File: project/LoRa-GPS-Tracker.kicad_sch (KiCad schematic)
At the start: 57 parts, among them IC101 MCP73831-2-OT, IC102 MCP100-300D, IC103 FT230XS, IC104 NCP705MT30TCG, M101 SIM28ML, M102 RAK3172, Q101 BSS123, Q102 TP0610K, Q103 BSH205G2VL, SW102 ON/OFF, X101 DEBUG, X102 Conn_Coaxial, X103 BATTERY, X3 DEBUG

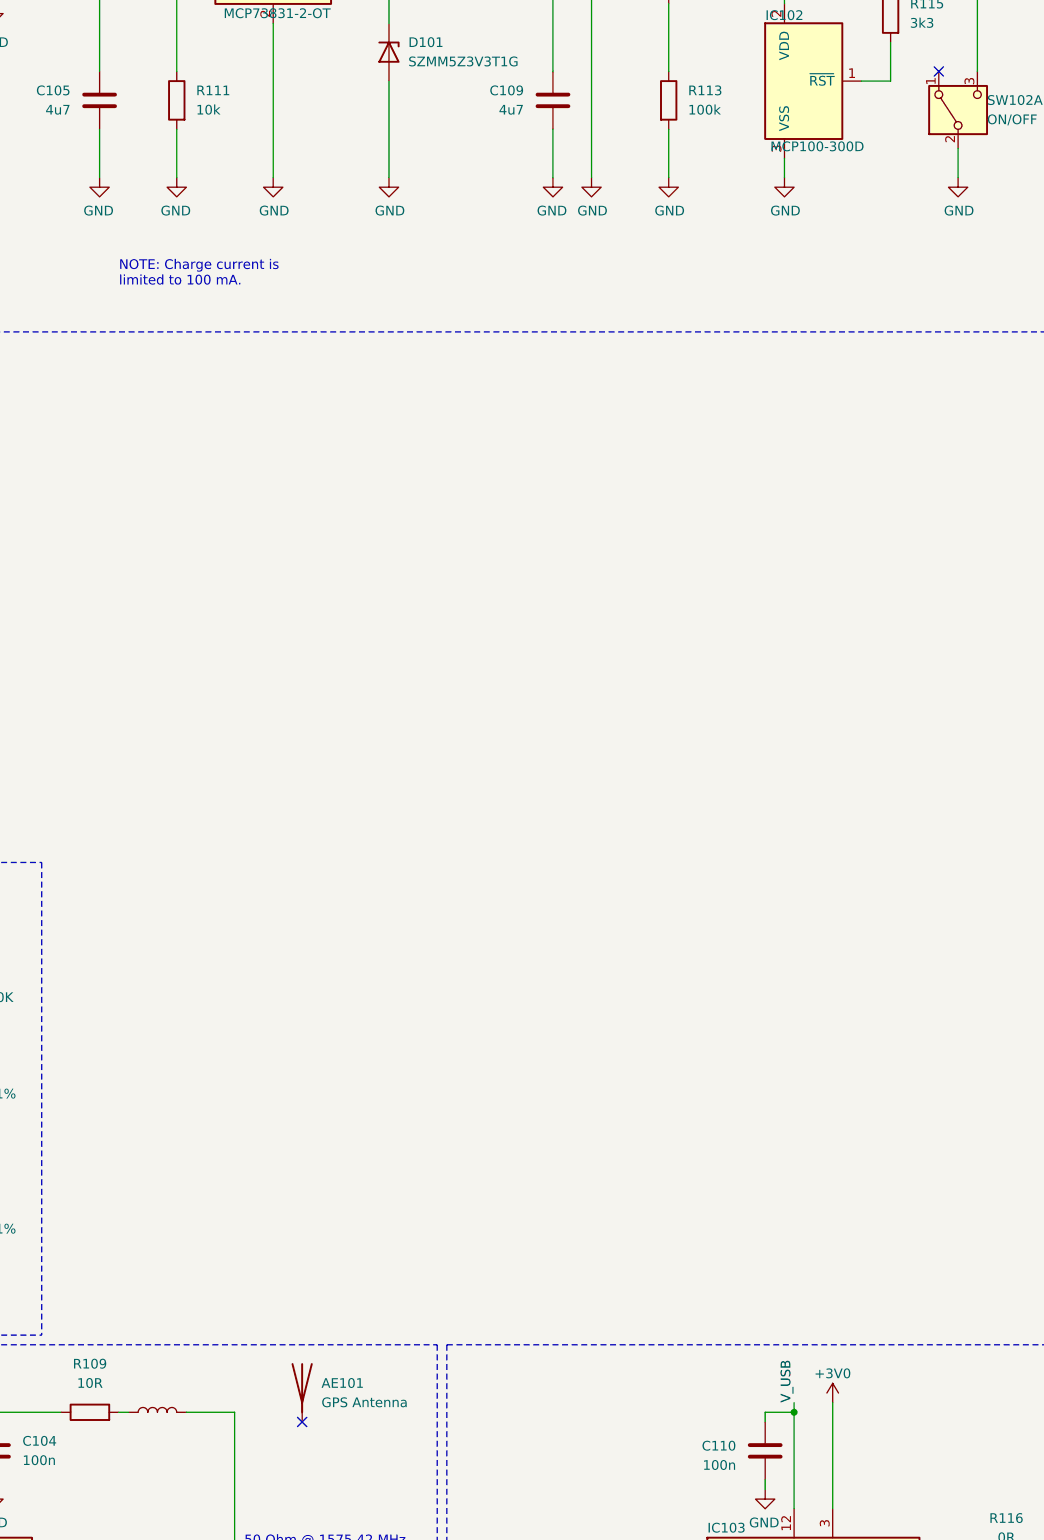
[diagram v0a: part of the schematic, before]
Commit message: Add missing part numbers and datasheets
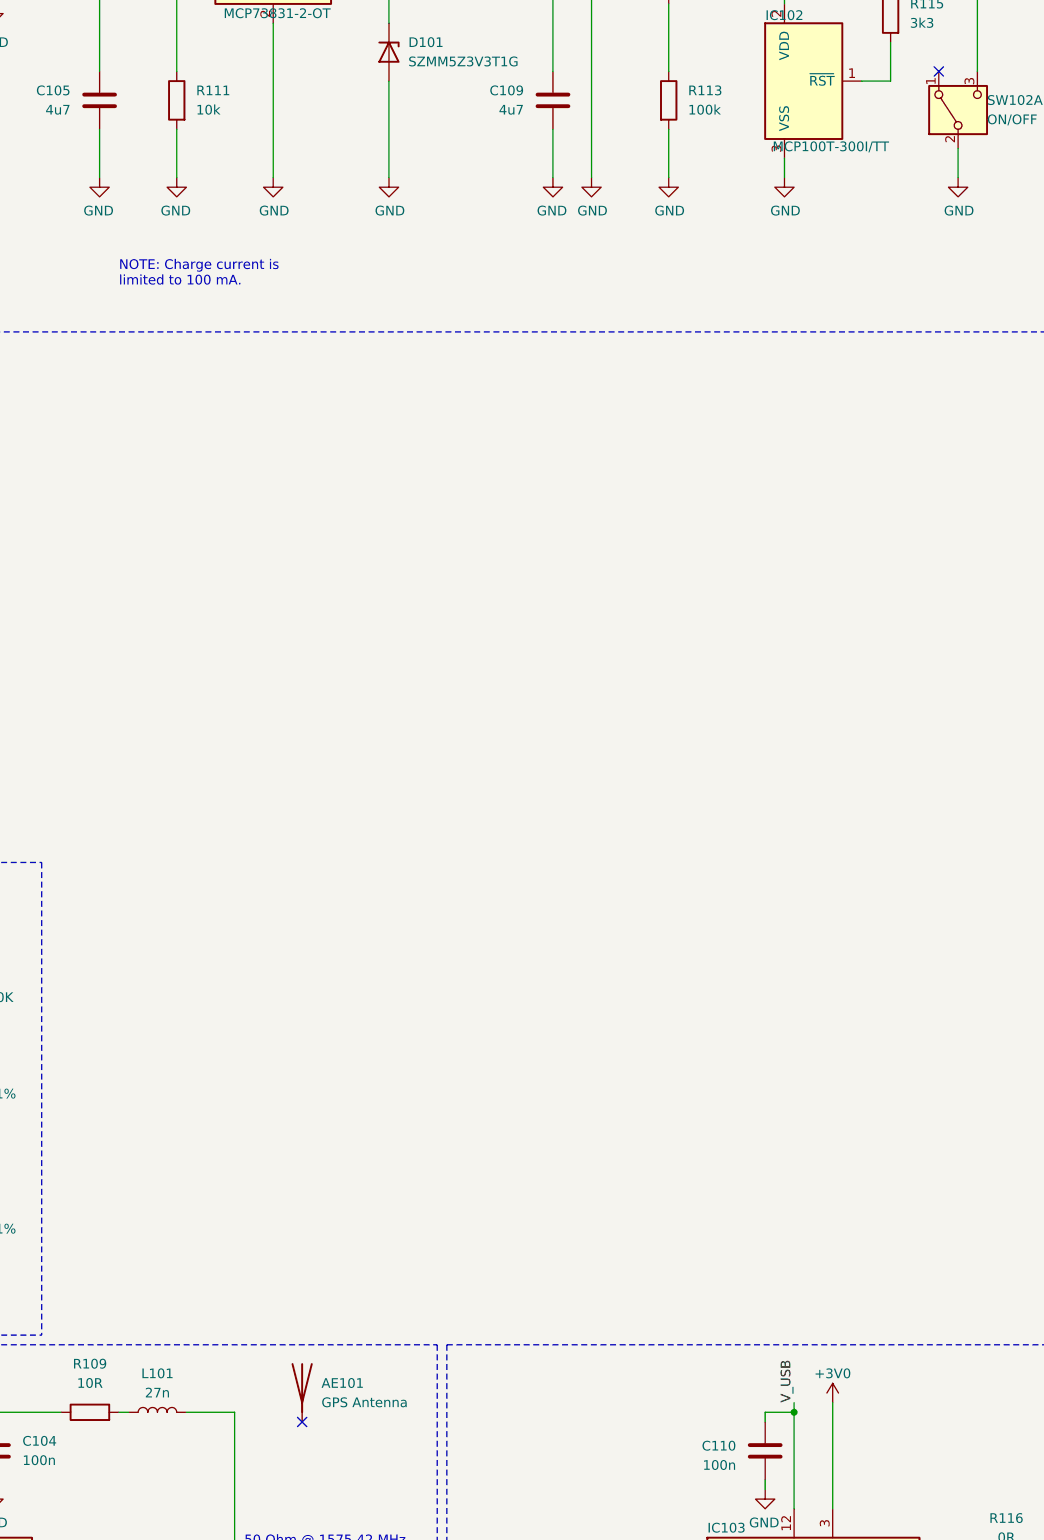
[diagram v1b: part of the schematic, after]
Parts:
- IC102: value MCP100-300D -> MCP100T-300I/TT
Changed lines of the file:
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@@
 			)
 		)
-		(property "Value" "MCP100-300D"
-			(at 174.498 59.436 0)
+		(property "Value" "MCP100T-300I/TT"
+			(at 176.276 59.436 0)
 			(effects
 				(font
@@
 			)
 		)
-		(property "Datasheet" "~"
+		(property "Datasheet" "https://www.mouser.de/datasheet/2/40/AVX_E_1004627-3313018.pdf"
 			(at 106.68 222.25 0)
 			(effects
@@
 		(fields_autoplaced yes)
 		(property "Reference" "L101"
-			(at 87.63 226.06 0)
+			(at 87.63 220.98 90)
 			(effects
 				(font
 					(size 1.27 1.27)
 				)
-				(hide yes)
 			)
 		)
 		(property "Value" "27n"
-			(at 87.63 226.06 0)
+			(at 87.63 223.52 90)
 			(effects
 				(font
 					(size 1.27 1.27)
 				)
-				(hide yes)
 			)
 		)
@@
 			(at 87.63 226.06 0)
 			(effects
+				(font
+					(size 1.27 1.27)
+				)
+				(hide yes)
+			)
+		)
+		(property "CONFIG" ""
+			(at 87.63 226.06 0)
+			(effects

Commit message: Make it possible to power cycle the GPS module
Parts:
- added Q104: TP0610K, Package_TO_SOT_SMD:SOT-23, symbol Transistor_FET:BSS84
- added R122: 100k, Resistor_SMD:R_0402_1005Metric_Pad0.72x0.64mm_HandSolder, symbol Device:R
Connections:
- net +3V0: now also Q104.2 (S), R122.1; no longer C101.1, C102.1, M101.8 (VCC)
- net GPS_E: now reaches M102.3 (ADC5)
- net GPS_E: now also Q104.1 (G), R122.2
- new net: C101.1, C102.1, M101.8 (VCC), Q104.3 (D)
- no-connect marks 29 -> 28
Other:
- moved on the sheet: C103, Q101, Q102, R101, R104, R105, R106

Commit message: Add I2C accelerometer
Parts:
- added C112: 100n, Capacitor_SMD:C_0402_1005Metric_Pad0.74x0.62mm_HandSolder, symbol Device:C
- added IC105: LIS2DH, Package_LGA:LGA-14_2x2mm_P0.35mm_LayoutBorder3x4y, symbol Sensor_Motion:LIS2DH
- added R115, R117: 3k3, Resistor_SMD:R_0402_1005Metric_Pad0.72x0.64mm_HandSolder, symbol Device:R
- R101: renamed from R102; Mfr. Bourns -> Vishay / Dale; Mfr. No. CR0805-J/-000ELF -> CRCW04020000Z0EDC; Order Number 652-CR0805-J/-000ELF -> 71-CRCW04020000Z0EDC
- R102: renamed from R103; Mfr. Bourns -> Vishay / Dale; Mfr. No. CR0805-J/-000ELF -> CRCW04020000Z0EDC; Order Number 652-CR0805-J/-000ELF -> 71-CRCW04020000Z0EDC
- R107: renamed from R110; Mfr. Bourns -> Vishay / Dale; Mfr. No. CR0805-J/-000ELF -> CRCW04020000Z0EDC; Order Number 652-CR0805-J/-000ELF -> 71-CRCW04020000Z0EDC
- R113: renamed from R116; Mfr. Bourns -> Vishay / Dale; Mfr. No. CR0805-J/-000ELF -> CRCW04020000Z0EDC; Order Number 652-CR0805-J/-000ELF -> 71-CRCW04020000Z0EDC
- R114: renamed from R117; Mfr. Bourns -> Vishay / Dale; Mfr. No. CR0805-J/-000ELF -> CRCW04020000Z0EDC; Order Number 652-CR0805-J/-000ELF -> 71-CRCW04020000Z0EDC
- R118: renamed from R101; now fitted
- X102: Mfr. Molex -> TE Connectivity / Linx Technologies; Mfr. No. 73412-0110 -> CONMHF1-SMD-G-T; Order Number 538-73412-0110 -> 712-CONMHF1-SMD-G-T
- renumbered C104 to C103, C105 to C104, C106 to C105, C107 to C106, C108 to C107, C109 to C108, C110 to C109, C111 to C110, C112 to C111, C103 to C115, D103 to D102, Q104 to Q101, Q103 to Q102, Q101 to Q103, Q102 to Q104, R122 to R103, R107 to R104, R108 to R105, R109 to R106, R111 to R108, R112 to R109, R113 to R110, R114 to R111, R115 to R112, R118 to R116, R120 to R119, R119 to R120, R104 to R121, R121 to R122, R105 to R123, R106 to R124, SW102 to SW101
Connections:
- net +3V0: now also C112.1, IC105.4 (~{CS}), IC105.7 (Vdd_IO), IC105.8 (Vdd), R115.1, R117.1
- net GND: now also C112.2, IC105.10 (GND), IC105.11 (GND), IC105.12 (GND), IC105.13 (GND), IC105.14 (GND), IC105.9 (GND)
- net at M102.10 (SDA): now also IC105.2 (SDA/SDI), R117.2
- net INT: now reaches M102.26 (ADC3)
- net INT: now also IC105.6 (INT1)
- net at M102.9 (SCL): now also IC105.1 (SCL/SPC), R115.2
- no-connect marks 28 -> 27
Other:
- moved on the sheet: C104

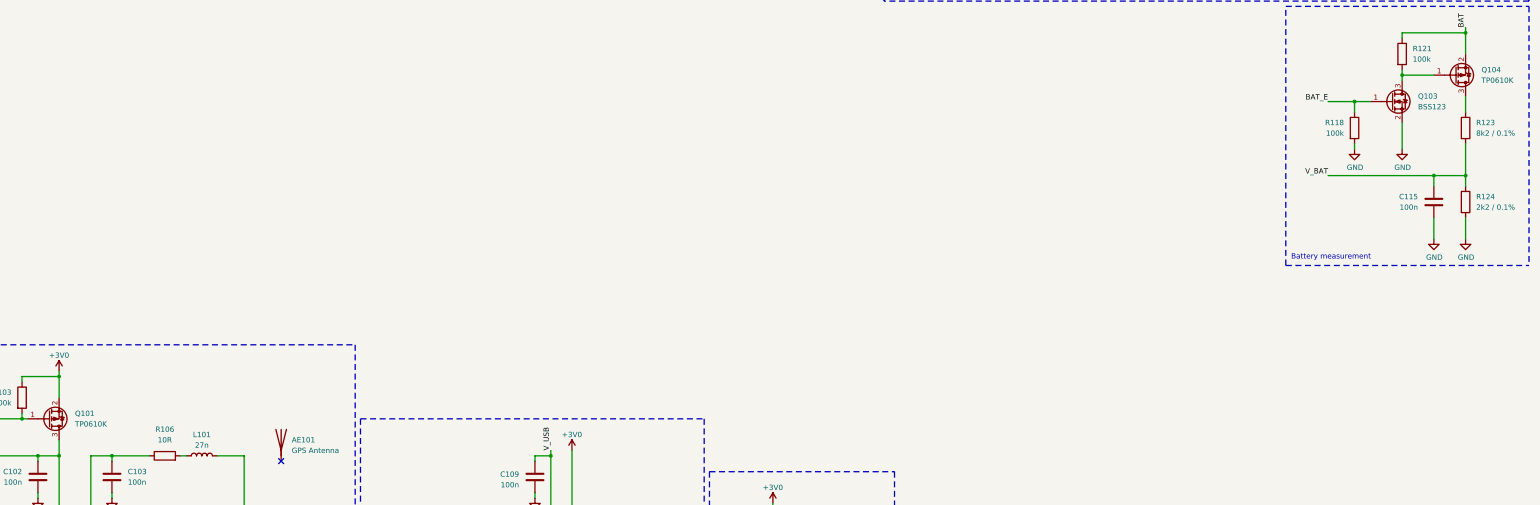
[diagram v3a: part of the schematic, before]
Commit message: Fix wrong package for CC resistors
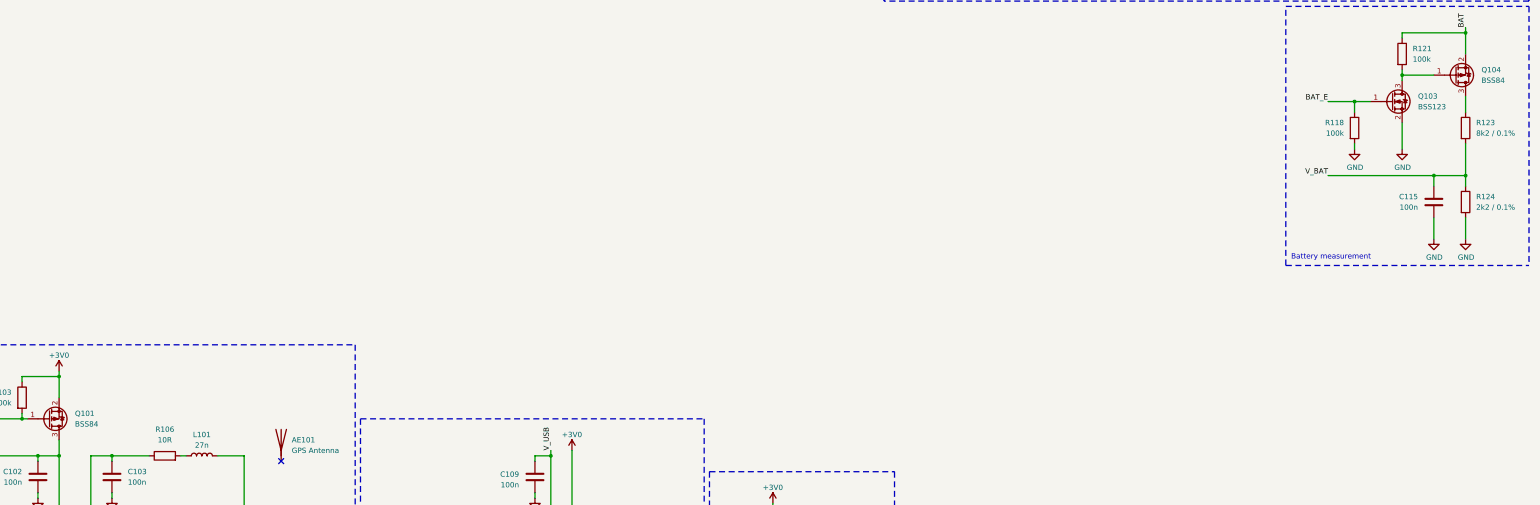
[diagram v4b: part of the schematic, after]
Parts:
- Q101, Q104: value TP0610K -> BSS84; Mfr. Vishay Semiconductors -> onsemi / Fairchild; Mfr. No. TP0610K-T1-GE3 -> BSS84; Order Number 781-TP0610K-T1-GE3 -> 512-BSS84
- R104, R105: footprint Resistor_SMD:R_0603_1608Metric -> Resistor_SMD:R_0402_1005Metric_Pad0.72x0.64mm_HandSolder; Mfr. No. CRCW06035K10FKEA -> RC0402JR-075K1L; Order Number 71-CRCW0603-5.1K-E3 -> 603-RC0402JR-075K1L
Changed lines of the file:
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@@
 			)
 		)
-		(property "Value" "TP0610K"
+		(property "Value" "BSS84"
 			(at 394.97 135.89 0)
 			(effects
@@
 			)
 		)
-		(property "Datasheet" "http://assets.nexperia.com/documents/data-sheet/BSS84.pdf"
+		(property "Datasheet" "https://www.mouser.de/datasheet/2/308/1/BSS84_D-2310226.pdf"
 			(at 388.62 134.62 0)
 			(effects
@@
 			)
 		)
-		(property "Mfr." "Vishay Semiconductors"
+		(property "Mfr." "onsemi / Fairchild"
 			(at 388.62 134.62 0)
 			(effects
@@
 			)
 		)
-		(property "Mfr. No." "TP0610K-T1-GE3"
+		(property "Mfr. No." "BSS84"
 			(at 388.62 134.62 0)
 			(effects
@@
 			)
 		)
-		(property "Order Number" "781-TP0610K-T1-GE3"
+		(property "Order Number" "512-BSS84"
+			(at 388.62 134.62 0)
+			(effects
+				(font
+					(size 1.27 1.27)
+				)
+				(hide yes)
+			)
+		)
+		(property "Order No." ""
+			(at 388.62 134.62 0)
+			(effects
+				(font
+					(size 1.27 1.27)
+				)
+				(hide yes)
+			)
+		)
+		(property "CONFIG" ""
 			(at 388.62 134.62 0)
 			(effects
@@
 			)
 		)
-		(property "Value" "TP0610K"
+		(property "Value" "BSS84"
 			(at 57.15 218.44 0)
 			(effects
@@
 			)
 		)
-		(property "Datasheet" "http://assets.nexperia.com/documents/data-sheet/BSS84.pdf"
+		(property "Datasheet" "https://www.mouser.de/datasheet/2/308/1/BSS84_D-2310226.pdf"
 			(at 50.8 217.17 0)
 			(effects
@@
 			)
 		)
-		(property "Mfr." "Vishay Semiconductors"
+		(property "Mfr." "onsemi / Fairchild"
 			(at 50.8 217.17 0)
 			(effects
@@
 			)
 		)
-		(property "Mfr. No." "TP0610K-T1-GE3"
+		(property "Mfr. No." "BSS84"
 			(at 50.8 217.17 0)
 			(effects
@@
 			)
 		)
-		(property "Order Number" "781-TP0610K-T1-GE3"
+		(property "Order Number" "512-BSS84"
+			(at 50.8 217.17 0)
+			(effects
+				(font
+					(size 1.27 1.27)
+				)
+				(hide yes)
+			)
+		)
+		(property "Order No." ""
+			(at 50.8 217.17 0)
+			(effects
+				(font
+					(size 1.27 1.27)
+				)
+				(hide yes)
+			)
+		)
+		(property "CONFIG" ""
 			(at 50.8 217.17 0)
 			(effects
@@
 			)
 		)
-		(property "Footprint" "Resistor_SMD:R_0603_1608Metric"
+		(property "Footprint" "Resistor_SMD:R_0402_1005Metric_Pad0.72x0.64mm_HandSolder"
 			(at 58.42 40.64 0)
 			(effects
@@
 			)
 		)
-		(property "Datasheet" "https://www.mouser.de/datasheet/2/447/PYu_RT_1_to_0_01_RoHS_L_15-3461507.pdf"
+		(property "Datasheet" "https://www.mouser.de/datasheet/2/447/YAGEO_PYu_RC_Group_51_RoHS_L_12-3313492.pdf"
 			(at 58.42 40.64 0)
 			(effects
@@
 			)
 		)
-		(property "Mfr. No." "CRCW06035K10FKEA"
+		(property "Mfr. No." "RC0402JR-075K1L"
 			(at 58.42 40.64 0)
 			(effects
@@
 			)
 		)
-		(property "Order Number" "71-CRCW0603-5.1K-E3"
+		(property "Order Number" "603-RC0402JR-075K1L"
 			(at 58.42 40.64 0)
 			(effects
@@
 			)
 		)
-		(property "Footprint" "Resistor_SMD:R_0603_1608Metric"
+		(property "Footprint" "Resistor_SMD:R_0402_1005Metric_Pad0.72x0.64mm_HandSolder"
 			(at 58.42 38.1 0)
 			(effects
@@
 			)
 		)
-		(property "Datasheet" "https://www.mouser.de/datasheet/2/447/PYu_RT_1_to_0_01_RoHS_L_15-3461507.pdf"
+		(property "Datasheet" "https://www.mouser.de/datasheet/2/447/YAGEO_PYu_RC_Group_51_RoHS_L_12-3313492.pdf"
 			(at 58.42 38.1 0)
 			(effects
@@
 			)
 		)
-		(property "Mfr. No." "CRCW06035K10FKEA"
+		(property "Mfr. No." "RC0402JR-075K1L"
 			(at 58.42 38.1 0)
 			(effects
@@
 			)
 		)
-		(property "Order Number" "71-CRCW0603-5.1K-E3"
+		(property "Order Number" "603-RC0402JR-075K1L"
 			(at 58.42 38.1 0)
 			(effects
